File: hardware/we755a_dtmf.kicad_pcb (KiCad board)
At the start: 2 copper layers, 49 x 82.3 mm, 52 parts, among them J1 Conn_01x06_Male, J3 Conn_02x10_Odd_Even, U1 AVR128DA28-I/SS, U2 MT8870, U3 H11AA1, U4 LAA108, U5 LAA108, U6 LAA108, U7 LAA108, U8 LAA108, Y1 32.767KHz, Y2 3.579545MHZ

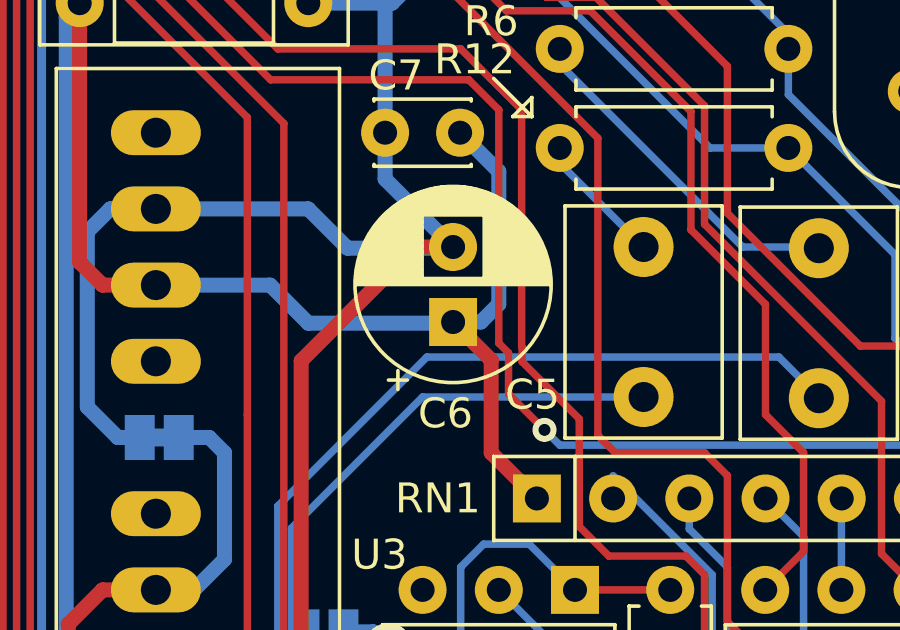
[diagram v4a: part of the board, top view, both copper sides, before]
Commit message: Change C6 from electrolytic to ceramic.
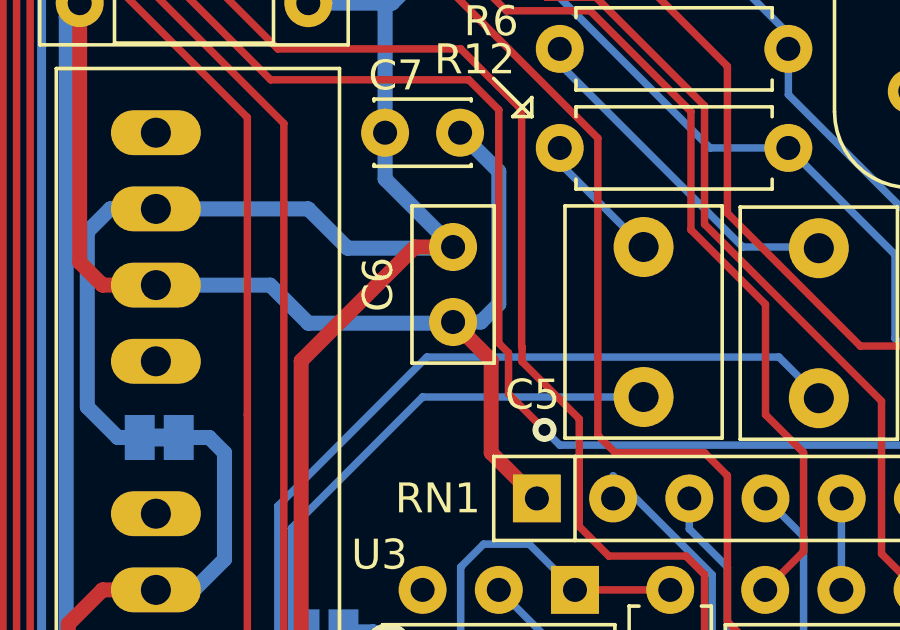
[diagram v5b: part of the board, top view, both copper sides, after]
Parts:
- C6: value 10uF 25V -> 10uf / 10V; footprint Capacitor_THT:CP_Radial_D6.3mm_P2.50mm -> Capacitor_THT:C_Disc_D5.0mm_W2.5mm_P2.50mm
